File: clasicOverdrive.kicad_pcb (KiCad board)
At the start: 2 copper layers, 48.9 x 31.3 mm, 34 parts, among them U2 LM4562

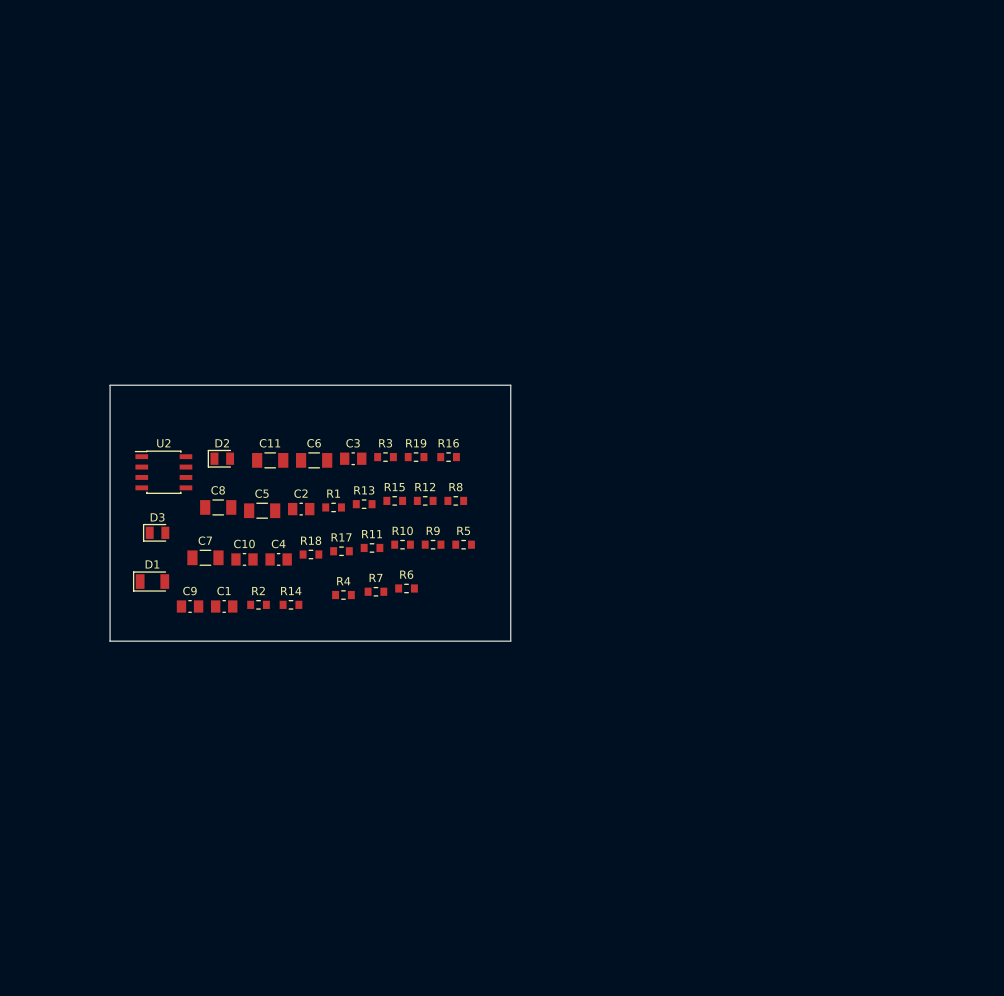
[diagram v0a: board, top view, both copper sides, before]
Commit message: all footprints added and layout of pcb complete
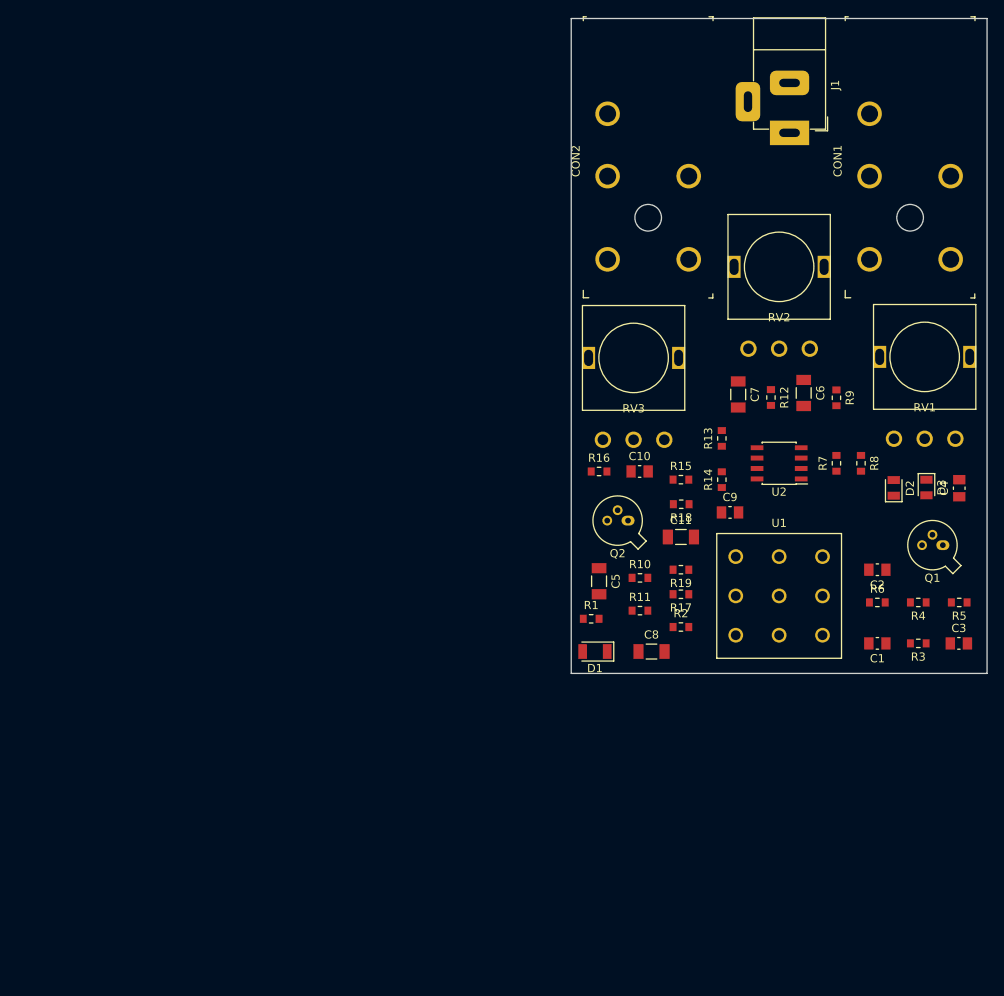
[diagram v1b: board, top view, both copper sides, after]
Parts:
- added CON1: SN49B12B, digikey-footprints:Headphone_Jack_6.35mm_RA49B14B, F.Cu at (209.0, 57.2)
- added CON2: SN49B12B, digikey-footprints:Headphone_Jack_6.35mm_RA49B14B, F.Cu at (177.0, 57.2)
- added J1: Jack-DC, Connector_Audio:Jack_Horizontal, F.Cu at (194.3, 46.9)
- added Q1: 2N2222, Package_TO_SOT_THT:TO-18-3, F.Cu at (213.0, 97.2)
- added Q2: 2N2222, Package_TO_SOT_THT:TO-18-3, F.Cu at (174.6, 94.2)
- added RV1: 500k, clasicOverdrive:Pot_series_296, F.Cu at (210.8, 84.2)
- added RV2: 25k, clasicOverdrive:Pot_series_296, F.Cu at (193.0, 73.2)
- added RV3: 100k, clasicOverdrive:Pot_series_296, F.Cu at (175.3, 84.4)
- added U1: foot_switch, clasicOverdrive:FS57003PLT2B2M2QE, F.Cu at (193.0, 103.4)
- moved D3 94.1 mm to (211.0, 90.2), turned to 270 degrees
- moved C4 83.6 mm to (215.0, 90.3), turned to 90 degrees
- moved D2 82.1 mm to (207.0, 90.2), turned to 90 degrees
- moved C1 79.9 mm to (205.0, 109.2), turned to 180 degrees
- moved C3 77.4 mm to (215.0, 109.2)
- moved U2 75.2 mm to (193.0, 87.2), turned to 180 degrees
- moved C2 70.8 mm to (205.0, 100.2), turned to 180 degrees
- moved R4 70.2 mm to (210.0, 104.2), turned to 180 degrees
- moved R3 68.9 mm to (210.0, 109.2), turned to 180 degrees
- moved C7 68.1 mm to (188.0, 78.8), turned to 270 degrees
- moved C9 67.0 mm to (187.0, 93.2)
- moved R5 61.0 mm to (215.0, 104.2), turned to 180 degrees
- moved C6 60.4 mm to (196.0, 78.6), turned to 270 degrees
- moved R7 58.4 mm to (200.0, 87.2), turned to 90 degrees
- moved R6 57.5 mm to (205.0, 104.2)
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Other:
- board size 48.9 x 31.3 mm -> 50.8 x 80 mm

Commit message: after freeRouter run
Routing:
- net GND: track 0.00 -> 179.1 mm
- net +9V: track 0.00 -> 161.4 mm
- net +4V5: track 0.00 -> 98.6 mm, vias 0 -> 2
- net Net-(CON2-PadR): track 0.00 -> 62.4 mm
- net Net-(CON1-PadT): track 0.00 -> 50.5 mm
- net Net-(C3-Pad1): track 0.00 -> 43.7 mm
- net Net-(C2-Pad2): track 0.00 -> 40.1 mm
- net Net-(C4-Pad2): track 0.00 -> 38.6 mm
- net Net-(C1-Pad2): track 0.00 -> 28.2 mm
- net Net-(C11-Pad2): track 0.00 -> 27.1 mm, vias 0 -> 1
- net Net-(C6-Pad1): track 0.00 -> 25.4 mm
- net Net-(R14-Pad2): track 0.00 -> 22.4 mm
- net Net-(D1-Pad1): track 0.00 -> 18.2 mm
- net Net-(Q2-Pad1): track 0.00 -> 17.2 mm
- net Net-(C3-Pad2): track 0.00 -> 13.9 mm
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- added copper zone on B.Cu, net GND
- added copper zone on F.Cu, net GND
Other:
- net class Default: trace_width 0.25 -> 0.4; via_dia 0.8 -> 0.6; via_drill 0.4 -> 0.35
- rule via_min_drill: 0.3 -> 0.2
- rule via_min_size: 0.4 -> 0.2

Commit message: Board Finished
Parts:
- added MK1: Mounting_Hole, MountingHole:MountingHole_3.2mm_M3, F.Cu at (104.0, 146.2)
- added MK2: Mounting_Hole, MountingHole:MountingHole_3.2mm_M3, F.Cu at (146.0, 146.2)
- added MK3: Mounting_Hole, MountingHole:MountingHole_3.2mm_M3, F.Cu at (146.0, 71.2)
- added MK4: Mounting_Hole, MountingHole:MountingHole_3.2mm_M3, F.Cu at (104.0, 71.2)
- moved J1 119.7 mm to (114.1, 135.7), turned to 0 degrees
- moved R5 114.4 mm to (102.5, 125.2), turned to 90 degrees
- moved Q1 108.8 mm to (108.0, 125.7), turned to 270 degrees
- moved R4 108.3 mm to (103.0, 121.3), turned to 90 degrees
- moved CON1 106.2 mm to (125.0, 122.2), turned to 0 degrees
- moved R3 104.3 mm to (106.5, 122.2), turned to 0 degrees
- moved C1 94.3 mm to (111.5, 121.7), turned to 0 degrees
- moved C4 88.8 mm to (142.0, 140.7), turned to 0 degrees
- moved C3 87.8 mm to (134.0, 75.2)
- moved C6 86.3 mm to (110.0, 71.7), turned to 90 degrees
- moved R12 82.2 mm to (137.0, 140.2)
- moved R9 82.1 mm to (118.0, 75.7), turned to 0 degrees
- moved D3 81.6 mm to (142.0, 133.7), turned to 180 degrees
- moved D2 80.2 mm to (142.1, 137.2), turned to 0 degrees
- moved U1 77.1 mm to (125.0, 139.7)
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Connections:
- RV1 pad 4: (no net) -> GND
- RV1 pad 5: (no net) -> GND
- RV2 pad 4: (no net) -> GND
- RV2 pad 5: (no net) -> GND
- RV3 pad 4: (no net) -> GND
- RV3 pad 5: (no net) -> GND
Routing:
- net GND: track 179.1 -> 4.69 mm, vias 0 -> 2
- net Net-(C3-Pad2): track 13.9 -> 69.5 mm, vias 0 -> 1
- net Net-(C4-Pad2): track 38.6 -> 89.1 mm, vias 0 -> 1
- net Net-(C2-Pad2): track 40.1 -> 85.3 mm, vias 0 -> 3
- net Net-(C7-Pad1): track 6.83 -> 43.8 mm
- net Net-(C3-Pad1): track 43.7 -> 7.57 mm
- net +9V: track 161.4 -> 133.1 mm, vias 0 -> 1
- net +4V5: track 98.6 -> 126.5 mm, vias 2 -> 0
- net Net-(C11-Pad2): track 27.1 -> 54.9 mm, vias 1 -> 0
- net Net-(CON2-PadR): track 62.4 -> 35.5 mm
- net Net-(C10-Pad2): track 4.61 -> 29.9 mm, vias 0 -> 1
- net Net-(C6-Pad1): track 25.4 -> 46.3 mm, vias 0 -> 2
- net Net-(R8-Pad1): track 5.44 -> 24.5 mm, vias 1 -> 0
- net Net-(R15-Pad1): track 5.32 -> 19.4 mm
- net Net-(D1-Pad1): track 18.2 -> 4.49 mm
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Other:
- board size 50.8 x 80 mm -> 50 x 83 mm
- net class Default: trace_width 0.4 -> 0.6
- net class PWR added: clearance 0.2, trace_width 0.8, via_dia 0.6, via_drill 0.35

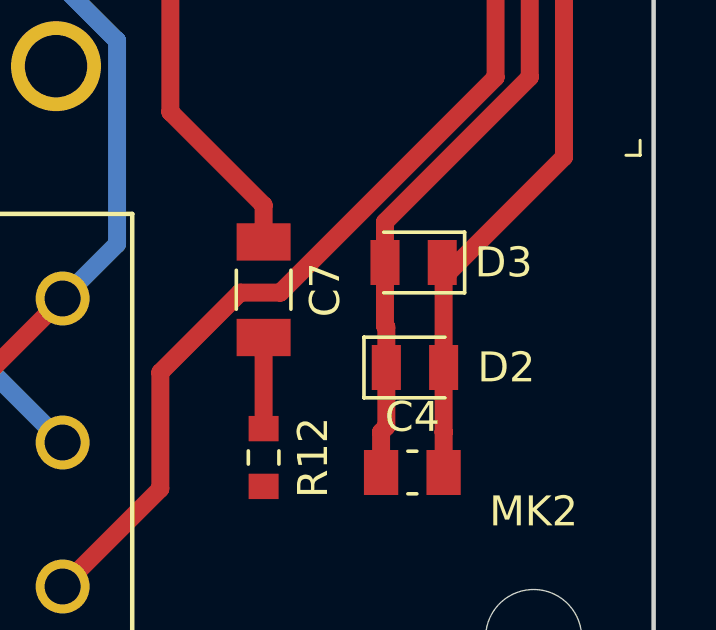
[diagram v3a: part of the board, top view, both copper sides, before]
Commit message: updated bom and footprint for the diodes@
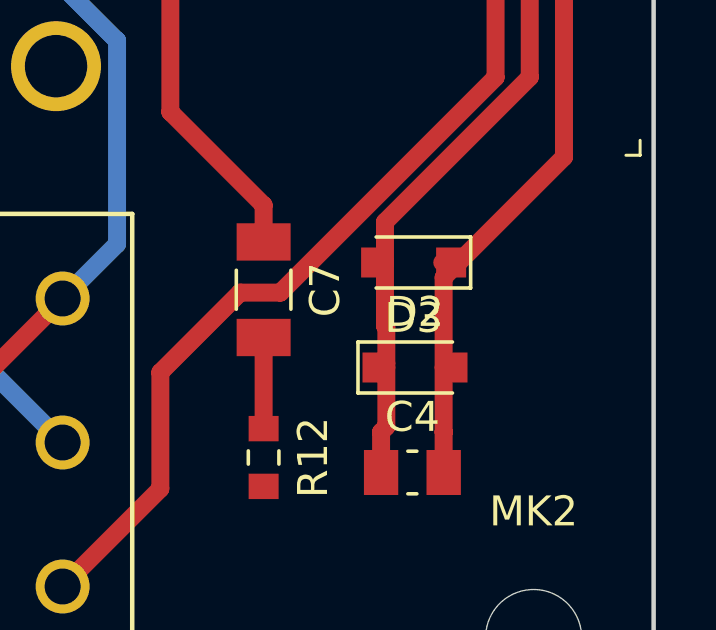
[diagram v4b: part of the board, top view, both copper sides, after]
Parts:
- D2, D3: footprint Diode_SMD:D_0805_2012Metric_Pad0.97x1.50mm_HandSolder -> Diode_SMD:D_SOD-323_HandSoldering
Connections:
- RV1 pad 4: GND -> (no net)
- RV1 pad 5: GND -> (no net)
- RV2 pad 4: GND -> (no net)
- RV2 pad 5: GND -> (no net)
- RV3 pad 4: GND -> (no net)
- RV3 pad 5: GND -> (no net)

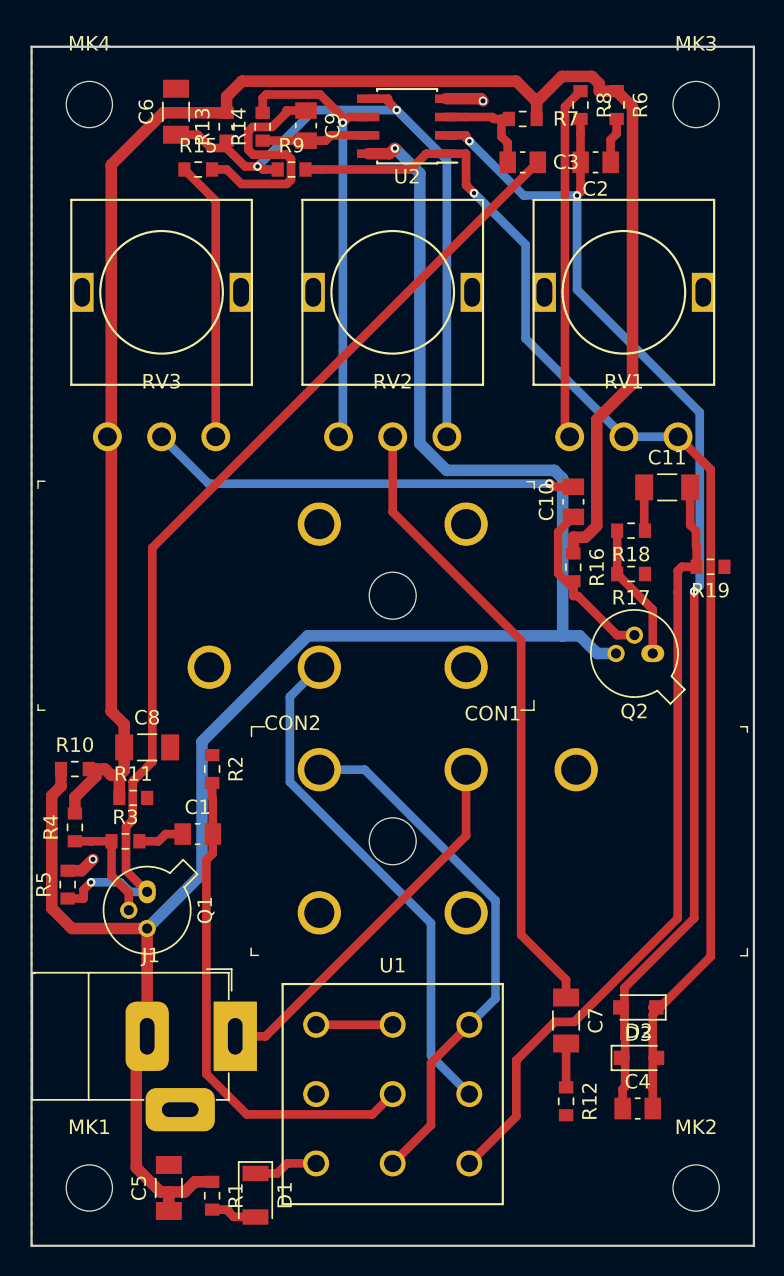
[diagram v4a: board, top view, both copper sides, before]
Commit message: update pcb and schematic with pads
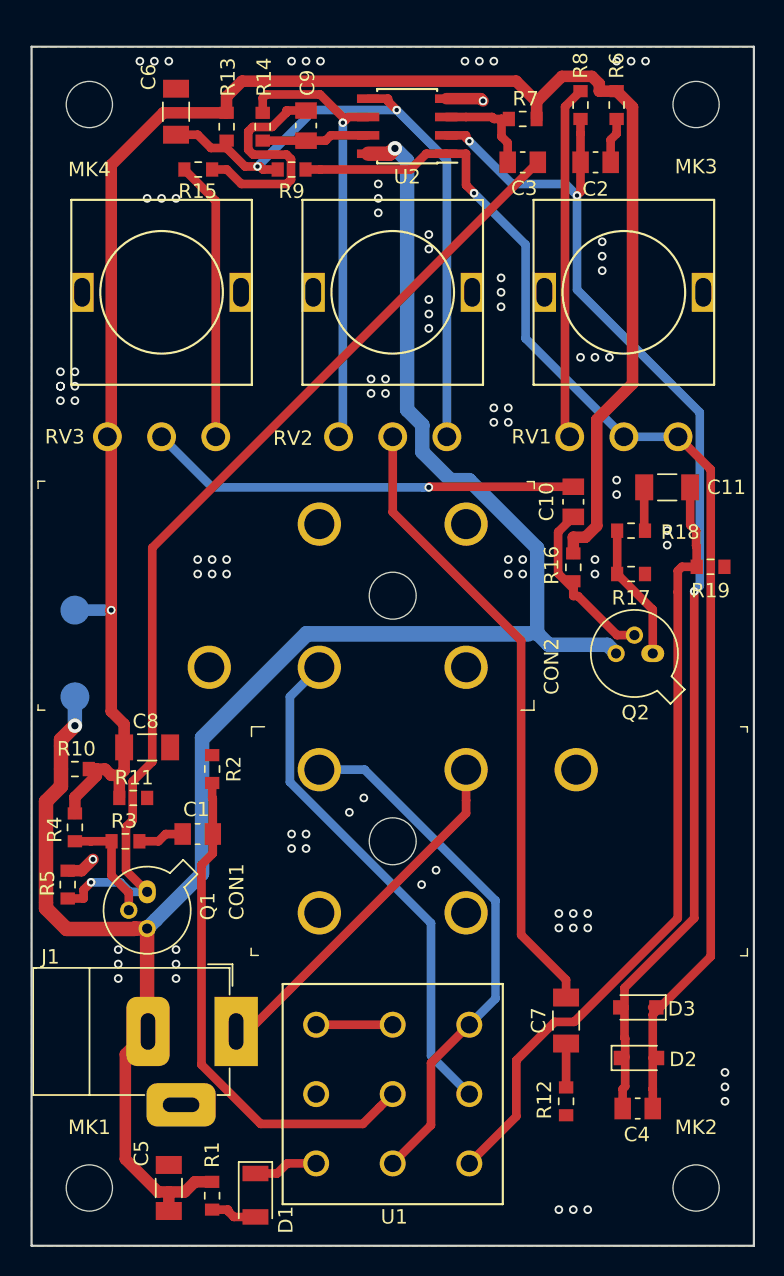
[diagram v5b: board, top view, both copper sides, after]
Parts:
- added TP1: 9V, TestPoint:TestPoint_Pad_D2.0mm, B.Cu at (103.0, 112.2)
- added TP2: 4V5, TestPoint:TestPoint_Pad_D2.0mm, B.Cu at (103.0, 106.2)
- moved J1 0.34 mm to (114.2, 135.4)
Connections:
- CON1 pad RB: Net-(CON1-PadRB) -> (no net)
- CON1 pad TB: Net-(CON1-PadTB) -> (no net)
- CON2 pad RB: Net-(CON2-PadRB) -> (no net)
- CON2 pad T: Net-(CON2-PadT) -> (no net)
- CON2 pad TB: Net-(CON2-PadTB) -> (no net)
- J1 pad 3: Net-(J1-Pad3) -> (no net)
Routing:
- net +9V: track 133.1 -> 173.0 mm, vias 1 -> 2
- net +4V5: track 126.5 -> 129.0 mm, vias 0 -> 1
- net Net-(CON1-PadR): track 26.3 -> 25.2 mm
- net Net-(C1-Pad2): track 35.0 -> 35.6 mm
- net GND: vias 2 -> 92
